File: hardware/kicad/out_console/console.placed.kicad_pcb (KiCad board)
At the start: 2 copper layers, 115 x 96 mm, 58 parts, among them J1 RaspberryPi_Pico_SMD_HandSold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, J10 JST_XH_B2B-XH-A_1x02_P2.50mm_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, J11 JST_XH_B2B-XH-A_1x02_P2.50mm_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, J12 JST_XH_B2B-XH-A_1x02_P2.50mm_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, J13 JST_XH_B2B-XH-A_1x02_P2.50mm_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, J14 JST_XH_B2B-XH-A_1x02_P2.50mm_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, J15 JST_XH_B2B-XH-A_1x02_P2.50mm_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, J16 JST_XH_B2B-XH-A_1x02_P2.50mm_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, J17 JST_XH_B2B-XH-A_1x02_P2.50mm_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, J18 JST_XH_B2B-XH-A_1x02_P2.50mm_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, J19 JST_XH_B2B-XH-A_1x02_P2.50mm_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, J2 IDC-Header_2x20_P2.54mm_Verti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, J20 JST_XH_B3B-XH-A_1x03_P2.50mm_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, J21 JST_XH_B3B-XH-A_1x03_P2.50mm_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, J22 PinHeader_2x04_P2.54mm_Vertic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, J3 JST_XH_B4B-XH-A_1x04_P2.50mm_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, J4 JST_XH_B3B-XH-A_1x03_P2.50mm_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, J5 JST_XH_B2B-XH-A_1x02_P2.50mm_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, J6 JST_XH_B8B-XH-A_1x08_P2.50mm_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, J7 JST_XH_B3B-XH-A_1x03_P2.50mm_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, J8 JST_XH_B2B-XH-A_1x02_P2.50mm_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, J9 JST_XH_B2B-XH-A_1x02_P2.50mm_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, U1 DIP-14_W7.62mm, U2 DIP-6_W7.62mm

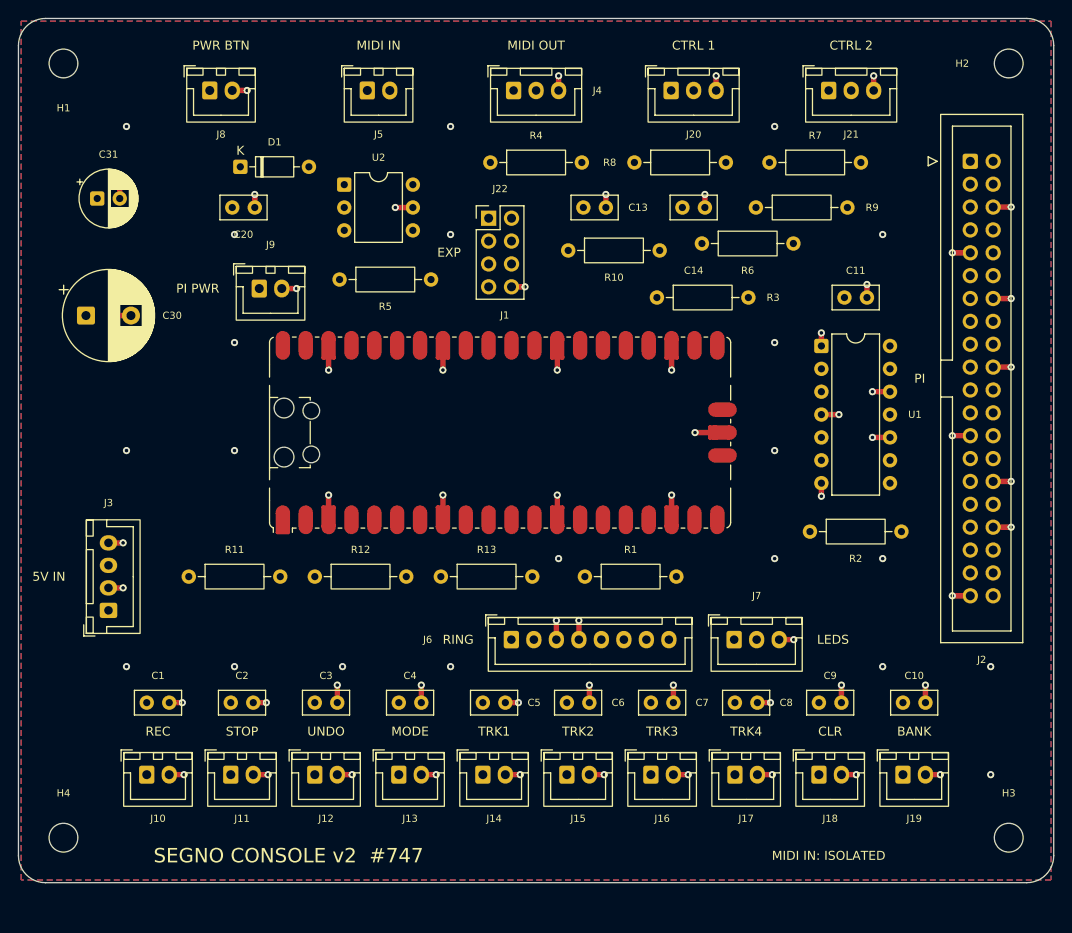
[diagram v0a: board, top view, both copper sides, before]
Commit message: fix(hardware): the console board fits the 100 x 100 mm fab tier
99.5 mm square, down from 115 x 96. Every prototype fab prices 2-layer boards
in a cheap tier that stops at 100 x 100, and the old width was over it for no
structural reason: the enclosure bay is 342 x 193, so nothing mechanical
wanted those 15 mm. 99.5 rather than 100.0 because Edge.Cuts is a 0.1 mm line
and a 100.0 outline measures 100.1 across the outside of it -- the half
millimetre costs nothing and means no CAM operator has to make that call.

Still 0 DRC violations and 0 unconnected, and the ratsnest went DOWN, from
1573 mm to 1473: a smaller board shortens every fan-out.

The width is now set by one thing, and it is worth knowing which: the ten
footswitch JSTs are 92.2 mm of outline at their pitch floor, so the board
cannot go below ~93 mm without giving up one connector per pedal. Everything
else fits inside that -- the widest other row is J3 + module + U1 + ribbon at
80.5 mm.

What the squeeze cost, and what it bought:

- U1 no longer fits between the module and the ribbon's column, so the module
  is pinned from the right at x 43. SW_BANK pays for it: 40.7 mm of the 42 mm
  hop limit, the tightest number on the board. The limit stays where it is
  rather than being relaxed to fit -- the next mm has to come from the
  floorplan, not the gate. The ratsnest budget is re-derived at 1610 mm.
- R2 stands upright in the 8 mm channel beside the module; a 12.3 mm axial
  cannot lie flat there and there is nowhere else for it.
- R5, R10 and D1 are hand-placed: the band is shoulder to shoulder and the
  spiral cannot find 12.3 mm of axial in range. D1 was the interesting one --
  it clamps the opto's LED, so it belongs in the isolated pocket with U2, R5
  and J5, but the spiral had parked it 15 mm away, straight across the only
  lane from J8 to J9, and PWR_BTN would not route at all. The isolation gate
  could not object: D1 shares the DIN-side nets, so it is exempt by
  construction.
- The designator 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
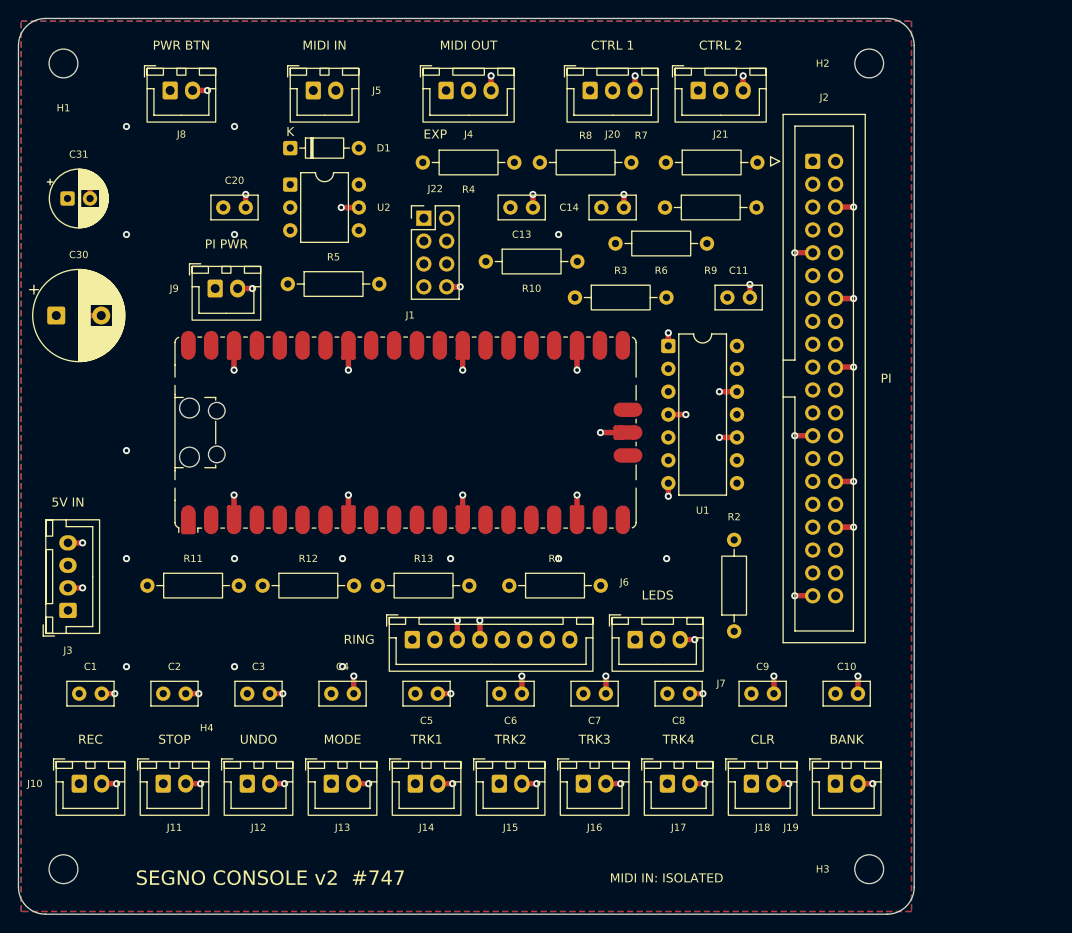
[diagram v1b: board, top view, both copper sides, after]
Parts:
- moved J2 17.5 mm to (188.2, 75.9)
- moved U1 17.0 mm to (172.2, 96.4)
- moved H3 15.9 mm to (194.5, 154.5)
- moved H2 15.5 mm to (194.5, 65.0)
- moved J21 14.5 mm to (175.5, 68.0)
- moved R2 13.9 mm to (179.5, 128.1), turned to 90 degrees
- moved C11 13.0 mm to (178.8, 91.0)
- moved R7 11.5 mm to (171.9, 76.0)
- moved J6 11.0 mm to (143.8, 129.0)
- moved J7 11.0 mm to (168.5, 129.0)
- moved J1 10.5 mm to (143.0, 106.0)
- moved R8 10.5 mm to (157.9, 76.0)
- moved R9 10.1 mm to (171.8, 81.0)
- moved R6 9.60 mm to (166.3, 85.0)
- moved R10 9.23 mm to (151.9, 87.0)
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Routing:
- net GND: track 113.1 -> 112.6 mm, vias 81 -> 75
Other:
- board size 115 x 96 mm -> 99.5 x 99.5 mm

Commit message: feat(hardware): bond the console board to the chassis, deliberately
The four mounting holes were bare NPTH -- no copper -- so the board floated
inside an earthed metal box. That was never a decision; it was the default
footprint. And it did not float in practice: the rear panel carries two USB 3.0
couplers, two DIN-5 sockets and two D-series TRS jacks, all bolted through
metal, and the TRS sleeves ARE this board's GND. A floating board in a box full
of bonded connector flanges is the worst case -- the loops exist anyway, through
long, undefined, high-impedance paths.

So: ONE hard DC bond, at H1. Top-left, the corner nearest where the outside
world arrives -- power button, MIDI, CTRL and ten footswitch leads all land
along the top edge -- and diagonally away from the ribbon, so an ESD strike on a
pedal cable reaches the case instead of travelling the 40-way into the Pi.

H2/H3/H4 get the option instead of the bond: an isolated pad with a 10 nF 2 kV
cap and a 1 M bleeder to GND, both DNF. A second DC bond would close a
mains-frequency loop (chassis -> Pi -> ribbon -> here -> chassis), which is where
hum comes from; a capacitor will not. 10 nF is ~318 k at 50 Hz, so no hum current
can flow, and ~0.16 ohm at 100 MHz, so ESD and RF still get a short path into the
case. The board ships single-point bonded and the pads exist so EMC testing can
change that with an iron rather than a respin.

H1..H4 are now REAL PARTS IN THE NETLIST rather than footprints the layout script
synthesised. One of them carries GND, and a chassis bond is a connection, so it
belongs in the source of truth. `_mounting_holes()` is deleted.

CHASSIS_BOND gates it: exactly one hole hard-bonded to GND -- two close the loop,
zero leaves the board floating -- and every other hole reaching ground only
through a capacitor AND a bleeder, never bare copper. Two negative controls, one
per half. The netlist self-test is now 12 controls, the layout one 8, all biting
the gate they name.

Layout fallout, all meas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
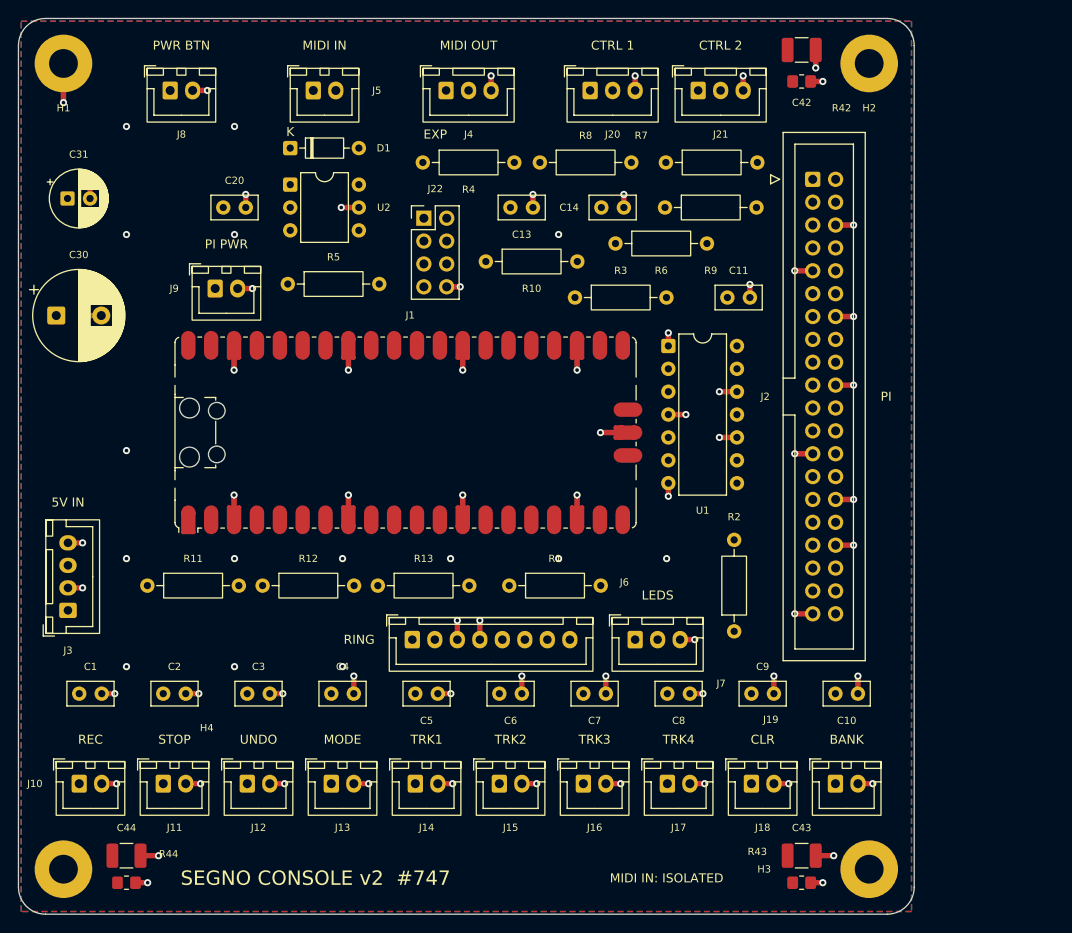
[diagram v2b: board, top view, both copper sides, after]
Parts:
- added C42: C_1210_3225Metric_Pad1.33x2.70mm_HandSolder, C_1210_3225Metric_Pad1.33x2.70mm_HandSolder, F.Cu at (187.0, 63.5)
- added C43: C_1210_3225Metric_Pad1.33x2.70mm_HandSolder, C_1210_3225Metric_Pad1.33x2.70mm_HandSolder, F.Cu at (187.0, 153.0)
- added C44: C_1210_3225Metric_Pad1.33x2.70mm_HandSolder, C_1210_3225Metric_Pad1.33x2.70mm_HandSolder, F.Cu at (112.0, 153.0)
- added R42: R_0805_2012Metric_Pad1.20x1.40mm_HandSolder, R_0805_2012Metric_Pad1.20x1.40mm_HandSolder, F.Cu at (187.0, 67.0)
- added R43: R_0805_2012Metric_Pad1.20x1.40mm_HandSolder, R_0805_2012Metric_Pad1.20x1.40mm_HandSolder, F.Cu at (187.0, 156.0)
- added R44: R_0805_2012Metric_Pad1.20x1.40mm_HandSolder, R_0805_2012Metric_Pad1.20x1.40mm_HandSolder, F.Cu at (112.0, 156.0)
- H1, H2, H3, H4: value MountingHole_3.2mm_M3 -> MountingHole_3.2mm_M3_Pad; footprint MountingHole_3.2mm_M3 -> MountingHole_3.2mm_M3_Pad
- moved J2 2.00 mm to (188.2, 77.9)
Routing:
- net GND: track 112.6 -> 127.0 mm, vias 75 -> 82

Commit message: fix(hardware): drop the SMD bond parts, and review the board for manufacture
The six surface-mount parts I added for the optional chassis bonds are gone.
They were a 10 nF cap and a 1 M bleeder per hole, unfitted by default, so EMC
testing could add an RF bond without a respin -- and nothing in through-hole
fits those corners, so they were SMD. That put six surface-mount parts on a
board that is hand-soldered through-hole on purpose, carried by every unit
built, for a bond that may never be wanted. H2/H3/H4 keep the plated pad and
nothing else; if a bond is ever needed a leaded cap solders from the pad to the
nearest ground via, which is a bench job on one board rather than a BOM line on
all of them. CHASSIS_BOND now gates that the other three holes are wired to
NOTHING -- a second path to ground through anything at all fails.

The only SMD left is J1, the Pico module, which is settled.

THE ENCLOSURE NOW MATCHES THE BOARD

The plate was drilling an 85 x 87 M3 rectangle measured off the V1 Pro Micro
board, while this board's holes are on 89.5 x 89.5. Both parts were unordered,
so it cost nothing -- once, and only because someone thought to look. The plate
now drills 89.5 x 89.5, reserves the real 99.5 x 99.5 outline, and the station
is labelled CONSOLE_BOARD rather than MAIN_BOARD, because the V1 board stays
with the standalone pedal.

It is a seam now, not a copied number: console_board_pcb.py writes
out_console/console_board_mount.json and segno_enclosure.py's BOARD_MOUNT gate
reads it -- the mirror of the rear_io_stations.json handoff going the other way.
Both halves of the gate were proven to bite.

WHAT THE FAB REVIEW FOUND

- Silkscreen under the fab's floor. All 58 designators were stroked at 0.133 mm
  against JLCPCB's 0.15 mm minimum, where lines thin, break, or are dropped.
  KiCad's own minimum is 0.08 mm, so its DRC had nothing to say. Stroke is now
  h/5 (0.16 mm at the 0.8 mm text height) and SILK_FAB gates height and stroke.
- Router vias at the fab f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
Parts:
- removed C42, C43, C44: C_1210_3225Metric_Pad1.33x2.70mm_HandSolder, C_1210_3225Metric_Pad1.33x2.70mm_HandSolder
- removed R42, R43, R44: R_0805_2012Metric_Pad1.20x1.40mm_HandSolder, R_0805_2012Metric_Pad1.20x1.40mm_HandSolder
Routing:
- net GND: track 127.0 -> 117.0 mm, vias 82 -> 76

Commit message: fix(hardware): move the Pi link off GPIO4, which the NVMe board owns
The console does not have a bare Pi. A GeeekPi N07 NVMe board (B0CWD266XR) sits
under it, and it takes GPIO4 -- physical pin 7 -- which is exactly where the
Pi->Pico link's RX sat. That would have been a board that assembles, passes
every gate here, and cannot talk to its own MCU: two drivers on one pin, found
at first power-on with a scope, not before.

The link moves to GPIO12/13, physical pins 32/33: `dtoverlay=uart4-pi5`,
"Enable uart 4 on GPIOs 12-13. Pi 5 only." GPIO5 moves too even though nothing
was reported on it -- it is the other half of the pair the N07 sits on, and a
peripheral that claims one pin commonly claims its neighbour. Pins 32/33 are
also at the far end of the header, away from the first six positions everything
crowds into.

Nothing else collided. Pins 2/4 (5 V) are DELIBERATELY not connected here -- the
buck must not parallel the PMIC, which was already settled -- and pins 6/9 are
GND, which every board on a Pi shares by definition.

PI_RESERVED now carries the pins another board on this Pi has claimed, with WHO
claimed them, and _check() refuses to put a signal on one. Rails are exempt:
sharing 3V3 and GND is the point of a header. Its negative control puts the link
back on pin 7.

The overlay name is not portable and now says so: GPIO12/13 is uart4 on a Pi 5
and uart5 on a Pi 4, the same way GPIO4/5 was uart2 here and uart3 there.

Board: 0 DRC violations, 0 unconnected, ERC 0/0, 22 negative controls all
biting. Refs #747.
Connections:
- J2 pad 29: LINK_TX -> (no net)
- J2 pad 32: (no net) -> LINK_RX
- J2 pad 33: (no net) -> LINK_TX
- J2 pad 7: LINK_RX -> (no net)

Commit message: fix(hardware): put the Pi link mid-header, safe under either reading
The N07 observation was POSITIONAL -- "first row 1-3, second row 4-5" -- and a
count of positions reads the same from either end of the header. Taken from the
near end it is pins 2/4/6 + 7/9, which is what the link was moved off. Mirrored,
it lands on 39/37/35 + 34/32, which is exactly where the link had just been put.
Dodging one end by moving to the other end was not a fix, it was a coin toss.

So the link now sits in the MIDDLE: `dtoverlay=uart3-pi5`, "Enable uart 3 on
GPIOs 8-9. Pi 5 only." Physical pins 24 and 21 are positions 11 and 12 of their
rows, as far from both ends as this header gets, and correct under either
reading of the observation.

GPIO8/9 are SPI0's CE0 and MISO. Nothing on this Pi uses SPI0 -- screens are USB
and HDMI, the SSD is PCIe, MIDI and the link are UARTs -- but if an SPI device
ever arrives, this is the pair it will want, so it is written down.

PI_RESERVED now carries both readings: pin 7 as observed, and 32/33 as the
mirror-image suspects. Our remaining pins on that header are 8/10 (MIDI, uart0,
which has no alternative on a Pi 5), 18/22 (SWD), and grounds. Grounds may well
coincide with the N07's contacts and that is fine -- every board on a Pi shares
them, which is why the gate exempts rails.

Firmware note changes with it: uart3-pi5, not uart4-pi5. Still not portable to a
Pi 4, where GPIO8-9 is uart4.

0 DRC violations, 0 unconnected, ERC 0/0, 23 controls biting. Refs #747, #752.
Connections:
- J2 pad 21: (no net) -> LINK_TX
- J2 pad 24: (no net) -> LINK_RX
- J2 pad 32: LINK_RX -> (no net)
- J2 pad 33: LINK_TX -> (no net)
